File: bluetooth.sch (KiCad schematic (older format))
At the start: 4 parts

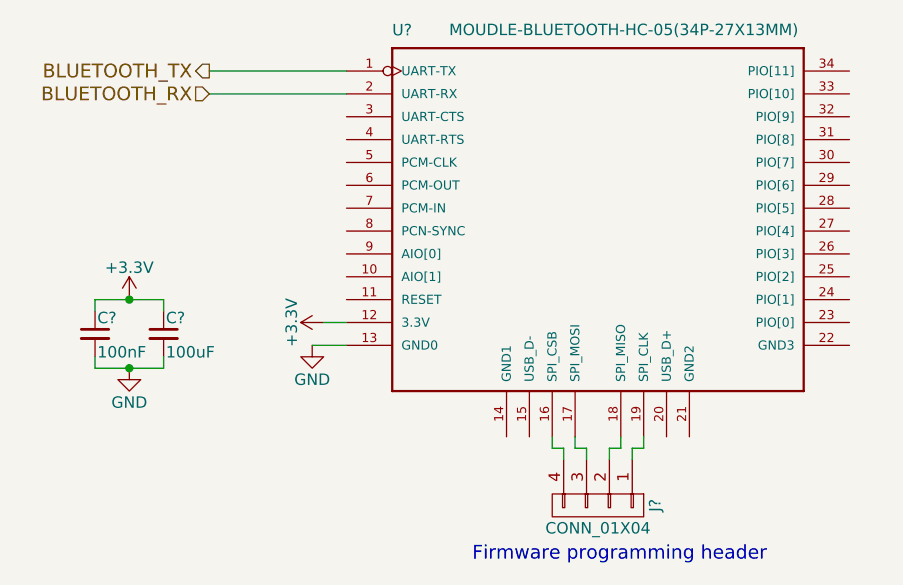
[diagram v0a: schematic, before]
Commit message: Make top-level connections between microcontroller and everything else
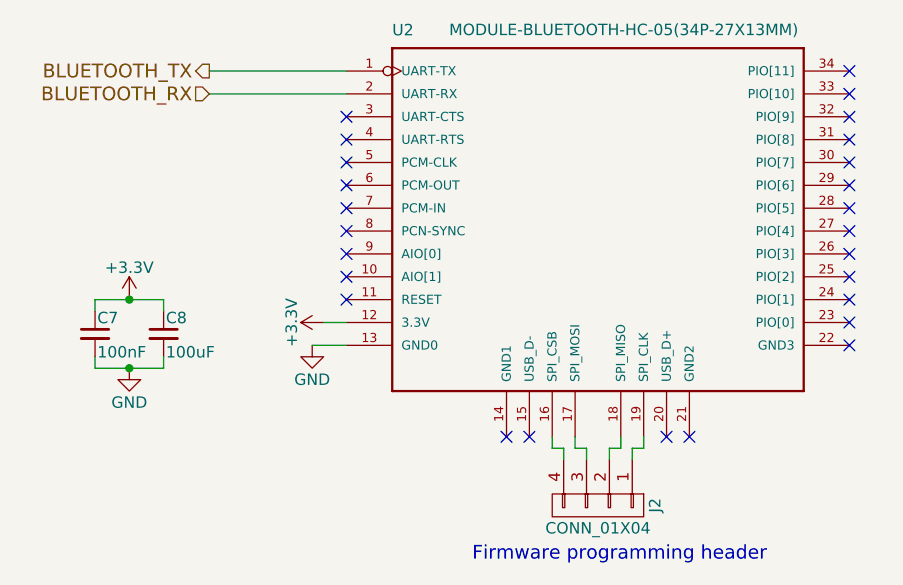
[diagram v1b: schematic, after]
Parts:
- U2: renamed from U?; value MOUDLE-BLUETOOTH-HC-05(34P-27X13MM) -> MODULE-BLUETOOTH-HC-05(34P-27X13MM); footprint BT34P-SMD-1.5-26.9X13.0X2.2MM -> (none)
- gave numbers to parts that had none: 3
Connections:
- no-connect marks 0 -> 26
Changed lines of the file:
@@
 $EndDescr
 $Comp
-L +3.3V #PWR?
+L +3.3V #PWR010
 U 1 1 599FF956
 P 4750 3550
-F 0 "#PWR?" H 4750 3400 50  0001 C CNN
+F 0 "#PWR010" H 4750 3400 50  0001 C CNN
 F 1 "+3.3V" H 4750 3690 50  0000 C CNN
 F 2 "" H 4750 3550 50  0001 C CNN
@@
 $EndComp
 $Comp
-L CONN_01X04 J?
+L CONN_01X04 J2
 U 1 1 599FF9B5
 P 5950 4350
-F 0 "J?" H 5950 4600 50  0000 C CNN
+F 0 "J2" H 5950 4600 50  0000 C CNN
 F 1 "CONN_01X04" V 6050 4350 50  0000 C CNN
 F 2 "" H 5950 4350 50  0001 C CNN
@@
 	4850 3550 4750 3550
 $Comp
-L GND #PWR?
+L GND #PWR011
 U 1 1 599FFB01
 P 4700 3650
-F 0 "#PWR?" H 4700 3400 50  0001 C CNN
+F 0 "#PWR011" H 4700 3400 50  0001 C CNN
 F 1 "GND" H 4700 3500 50  0000 C CNN
 F 2 "" H 4700 3650 50  0001 C CNN
@@
 BLUETOOTH_RX
 $Comp
-L C_Small C?
+L C_Small C8
 U 1 1 599FFDBC
 P 4050 3600
-F 0 "C?" H 4060 3670 50  0000 L CNN
+F 0 "C8" H 4060 3670 50  0000 L CNN
 F 1 "100uF" H 4060 3520 50  0000 L CNN
 F 2 "" H 4050 3600 50  0001 C CNN
@@
 $EndComp
 $Comp
-L C_Small C?
+L C_Small C7
 U 1 1 599FFE10
 P 3750 3600
-F 0 "C?" H 3760 3670 50  0000 L CNN
+F 0 "C7" H 3760 3670 50  0000 L CNN
 F 1 "100nF" H 3760 3520 50  0000 L CNN
 F 2 "" H 3750 3600 50  0001 C CNN
@@
 $EndComp
 $Comp
-L GND #PWR?
+L GND #PWR012
 U 1 1 599FFE4C
 P 3900 3750
-F 0 "#PWR?" H 3900 3500 50  0001 C CNN
+F 0 "#PWR012" H 3900 3500 50  0001 C CNN
 F 1 "GND" H 3900 3600 50  0000 C CNN
 F 2 "" H 3900 3750 50  0001 C CNN
@@
 $EndComp
 $Comp
-L +3.3V #PWR?
+L +3.3V #PWR013
 U 1 1 599FFE63
 P 3900 3450
-F 0 "#PWR?" H 3900 3300 50  0001 C CNN
+F 0 "#PWR013" H 3900 3300 50  0001 C CNN
 F 1 "+3.3V" H 3900 3590 50  0000 C CNN
 F 2 "" H 3900 3450 50  0001 C CNN
@@
 Connection ~ 3900 3450
 $Comp
-L MOUDLE-BLUETOOTH-HC-05(34P-27X13MM) U?
+L MOUDLE-BLUETOOTH-HC-05(34P-27X13MM) U2
 U 1 1 59A0DEC9
 P 5950 3100
-F 0 "U?" H 5050 3900 50  0000 L BNN
-F 1 "MOUDLE-BLUETOOTH-HC-05(34P-27X13MM)" H 5299 3901 50  0000 L BNN
-F 2 "BT34P-SMD-1.5-26.9X13.0X2.2MM" H 5950 3100 50  0001 L BNN
+F 0 "U2" H 5050 3900 50  0000 L BNN
+F 1 "MODULE-BLUETOOTH-HC-05(34P-27X13MM)" H 5299 3901 50  0000 L BNN
+F 2 "" H 5950 3100 50  0001 L BNN
 F 3 "None" H 5950 3100 50  0001 L BNN
 F 4 "HC-05" H 5950 3100 50  0001 L BNN "MP"
@@
 Text Notes 5400 4600 0    60   ~ 0
 Firmware programming header
+NoConn ~ 6350 4050
+NoConn ~ 6250 4050
+NoConn ~ 5650 4050
+NoConn ~ 5550 4050
+NoConn ~ 4850 3450
+NoConn ~ 4850 3350
+NoConn ~ 4850 3250
+NoConn ~ 4850 3150
+NoConn ~ 4850 3050
+NoConn ~ 4850 2950
+NoConn ~ 4850 2850
+NoConn ~ 4850 2750
+NoConn ~ 4850 2650
+NoConn ~ 7050 2450
+NoConn ~ 7050 2550
+NoConn ~ 7050 2650
+NoConn ~ 7050 2750
+NoConn ~ 7050 2850
+NoConn ~ 7050 2950
+NoConn ~ 7050 3050
+NoConn ~ 7050 3150
+NoConn ~ 7050 3250
+NoConn ~ 7050 3350
+NoConn ~ 7050 3450
+NoConn ~ 7050 3550
+NoConn ~ 7050 3650
 $EndSCHEMATC

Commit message: Assigned some footprints and added CR1225 holder footprint
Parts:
- C7: footprint (none) -> Capacitors_SMD:C_0603
- C8: footprint (none) -> Capacitors_Tantalum_SMD:CP_Tantalum_Case-B_EIA-3528-21_Reflow
- J2: footprint (none) -> Pin_Headers:Pin_Header_Straight_1x04_Pitch2.54mm
- U2: footprint (none) -> bluetooth_hc-05:BT34P-SMD-1.5-26.9X13.0X2.2MM
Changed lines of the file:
@@
 F 0 "J2" H 5950 4600 50  0000 C CNN
 F 1 "CONN_01X04" V 6050 4350 50  0000 C CNN
-F 2 "" H 5950 4350 50  0001 C CNN
+F 2 "Pin_Headers:Pin_Header_Straight_1x04_Pitch2.54mm" H 5950 4350 50  0001 C CNN
 F 3 "" H 5950 4350 50  0001 C CNN
 	1    5950 4350
@@
 F 0 "C8" H 4060 3670 50  0000 L CNN
 F 1 "100uF" H 4060 3520 50  0000 L CNN
-F 2 "" H 4050 3600 50  0001 C CNN
+F 2 "Capacitors_Tantalum_SMD:CP_Tantalum_Case-B_EIA-3528-21_Reflow" H 4050 3600 50  0001 C CNN
 F 3 "" H 4050 3600 50  0001 C CNN
 	1    4050 3600
@@
 F 0 "C7" H 3760 3670 50  0000 L CNN
 F 1 "100nF" H 3760 3520 50  0000 L CNN
-F 2 "" H 3750 3600 50  0001 C CNN
+F 2 "Capacitors_SMD:C_0603" H 3750 3600 50  0001 C CNN
 F 3 "" H 3750 3600 50  0001 C CNN
 	1    3750 3600
@@
 F 0 "U2" H 5050 3900 50  0000 L BNN
 F 1 "MODULE-BLUETOOTH-HC-05(34P-27X13MM)" H 5299 3901 50  0000 L BNN
-F 2 "" H 5950 3100 50  0001 L BNN
+F 2 "bluetooth_hc-05:BT34P-SMD-1.5-26.9X13.0X2.2MM" H 5950 3100 50  0001 L BNN
 F 3 "None" H 5950 3100 50  0001 L BNN
 F 4 "HC-05" H 5950 3100 50  0001 L BNN "MP"

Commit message: Create relevant BOM links, export digikey BOM
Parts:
- C8: MFR (none) -> AVX; MPN (none) -> F930J107MBA; SPN (none) -> 478-8156-1-ND; SPR (none) -> https://www.digikey.com.au/
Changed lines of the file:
@@
 U 1 1 599FF956
 P 4750 3550
-F 0 "#PWR010" H 4750 3400 50  0001 C CNN
-F 1 "+3.3V" H 4750 3690 50  0000 C CNN
-F 2 "" H 4750 3550 50  0001 C CNN
-F 3 "" H 4750 3550 50  0001 C CNN
+F 0 "#PWR010" H 4750 3400 50 0001 C CNN
+F 1 "+3.3V" H 4750 3690 50 0000 C CNN
+F 2 "" H 4750 3550 50 0001 C CNN
+F 3 "" H 4750 3550 50 0001 C CNN
 	1    4750 3550
 	0    -1   -1   0
@@
 U 1 1 599FF9B5
 P 5950 4350
-F 0 "J2" H 5950 4600 50  0000 C CNN
-F 1 "CONN_01X04" V 6050 4350 50  0000 C CNN
-F 2 "Pin_Headers:Pin_Header_Straight_1x04_Pitch2.54mm" H 5950 4350 50  0001 C CNN
-F 3 "" H 5950 4350 50  0001 C CNN
+F 0 "J2" H 5950 4600 50 0000 C CNN
+F 1 "CONN_01X04" V 6050 4350 50 0000 C CNN
+F 2 "Pin_Headers:Pin_Header_Straight_1x04_Pitch2.54mm" H 5950 4350 50 0001 C CNN
+F 3 "" H 5950 4350 50 0001 C CNN
+F 4 "" H 0 0 50 0001 C CNN "MFR"
+F 5 "" H 0 0 50 0001 C CNN "MPN"
+F 6 "" H 0 0 50 0001 C CNN "SPR"
+F 7 "" H 0 0 50 0001 C CNN "SPN"
+F 8 "" H 0 0 50 0001 C CNN "SPURL"
 	1    5950 4350
 	0    1    1    0
 $EndComp
+$Comp
+L GND #PWR011
+U 1 1 599FFB01
+P 4700 3650
+F 0 "#PWR011" H 4700 3400 50 0001 C CNN
+F 1 "GND" H 4700 3500 50 0000 C CNN
+F 2 "" H 4700 3650 50 0001 C CNN
+F 3 "" H 4700 3650 50 0001 C CNN
+	1    4700 3650
+	1    0    0    -1
+$EndComp
+$Comp
+L C_Small C8
+U 1 1 599FFDBC
+P 4050 3600
+F 0 "C8" H 4060 3670 50 0000 L CNN
+F 1 "100uF" H 4060 3520 50 0000 L CNN
+F 2 "Capacitors_Tantalum_SMD:CP_Tantalum_Case-B_EIA-3528-21_Reflow" H 4050 3600 50 0001 C CNN
+F 3 "http://datasheets.avx.com/F93.pdf" H 4050 3600 50 0001 C CNN
+F 4 "AVX" H 0 0 50 0001 C CNN "MFR"
+F 5 "F930J107MBA" H 0 0 50 0001 C CNN "MPN"
+F 6 "https://www.digikey.com.au/" H 0 0 50 0001 C CNN "SPR"
+F 7 "478-8156-1-ND" H 0 0 50 0001 C CNN "SPN"
+F 8 "" H 0 0 50 0001 C CNN "SPURL"
+	1    4050 3600
+	1    0    0    -1
+$EndComp
+$Comp
+L C_Small C7
+U 1 1 599FFE10
+P 3750 3600
+F 0 "C7" H 3760 3670 50 0000 L CNN
+F 1 "100nF" H 3760 3520 50 0000 L CNN
+F 2 "Capacitors_SMD:C_0603" H 3750 3600 50 0001 C CNN
+F 3 "" H 3750 3600 50 0001 C CNN
+F 4 "" H 0 0 50 0001 C CNN "MFR"
+F 5 "" H 0 0 50 0001 C CNN "MPN"
+F 6 "" H 0 0 50 0001 C CNN "SPR"
+F 7 "" H 0 0 50 0001 C CNN "SPN"
+F 8 "" H 0 0 50 0001 C CNN "SPURL"
+	1    3750 3600
+	1    0    0    -1
+$EndComp
+$Comp
+L GND #PWR012
+U 1 1 599FFE4C
+P 3900 3750
+F 0 "#PWR012" H 3900 3500 50 0001 C CNN
+F 1 "GND" H 3900 3600 50 0000 C CNN
+F 2 "" H 3900 3750 50 0001 C CNN
+F 3 "" H 3900 3750 50 0001 C CNN
+	1    3900 3750
+	1    0    0    -1
+$EndComp
+$Comp
+L +3.3V #PWR013
+U 1 1 599FFE63
+P 3900 3450
+F 0 "#PWR013" H 3900 3300 50 0001 C CNN
+F 1 "+3.3V" H 3900 3590 50 0000 C CNN
+F 2 "" H 3900 3450 50 0001 C CNN
+F 3 "" H 3900 3450 50 0001 C CNN
+	1    3900 3450
+	1    0    0    -1
+$EndComp
+$Comp
+L MOUDLE-BLUETOOTH-HC-05(34P-27X13MM) U2
+U 1 1 59A0DEC9
+P 5950 3100
+F 0 "U2" H 5050 3900 50 0000 L BNN
+F 1 "MODULE-BLUETOOTH-HC-05(34P-27X13MM)" H 5299 3901 50 0000 L BNN
+F 2 "bluetooth_hc-05:BT34P-SMD-1.5-26.9X13.0X2.2MM" H 5950 3100 50 0001 L BNN
+F 3 "None" H 5950 3100 50 0001 L BNN
+F 4 "HC-05" H 5950 3100 50 0001 L BNN "MP"
+F 5 "SOIC-14 " H 5950 3100 50 0001 L BNN "Package"
+F 6 "Unavailable" H 5950 3100 50 0001 L BNN "Availability"
+F 7 "None" H 5950 3100 50 0001 L BNN "Description"
+F 8 "" H 5950 3100 50 0001 L BNN "MF"
+F 9 "" H 0 0 50 0001 C CNN "MFR"
+F 10 "" H 0 0 50 0001 C CNN "MPN"
+F 11 "" H 0 0 50 0001 C CNN "SPR"
+F 12 "" H 0 0 50 0001 C CNN "SPN"
+F 13 "" H 0 0 50 0001 C CNN "SPURL"
+	1    5950 3100
+	1    0    0    -1
+$EndComp
+Text HLabel 4250 2450 0    60   Output ~ 0
+BLUETOOTH_TX
+Text HLabel 4250 2550 0    60   Input ~ 0
+BLUETOOTH_RX
+Text Notes 5400 4600 0    60   ~ 0
+Firmware programming header
 Wire Wire Line
 	6150 4050 6150 4100
@@
 Wire Wire Line
 	4850 3550 4750 3550
-$Comp
-L GND #PWR011
-U 1 1 599FFB01
-P 4700 3650
-F 0 "#PWR011" H 4700 3400 50  0001 C CNN
-F 1 "GND" H 4700 3500 50  0000 C CNN
-F 2 "" H 4700 3650 50  0001 C CNN
-F 3 "" H 4700 3650 50  0001 C CNN
-	1    4700 3650
-	1    0    0    -1
-$EndComp
 Wire Wire Line
 	4850 3650 4700 3650
@@
 Wire Wire Line
 	4850 2550 4250 2550
-Text HLabel 4250 2450 0    60   Output ~ 0
-BLUETOOTH_TX
-Text HLabel 4250 2550 0    60   Input ~ 0
-BLUETOOTH_RX
-$Comp
-L C_Small C8
-U 1 1 599FFDBC
-P 4050 3600
-F 0 "C8" H 4060 3670 50  0000 L CNN
-F 1 "100uF" H 4060 3520 50  0000 L CNN
-F 2 "Capacitors_Tantalum_SMD:CP_Tantalum_Case-B_EIA-3528-21_Reflow" H 4050 3600 50  0001 C CNN
-F 3 "" H 4050 3600 50  0001 C CNN
-	1    4050 3600
-	1    0    0    -1
-$EndComp
-$Comp
-L C_Small C7
-U 1 1 599FFE10
-P 3750 3600
-F 0 "C7" H 3760 3670 50  0000 L CNN
-F 1 "100nF" H 3760 3520 50  0000 L CNN
-F 2 "Capacitors_SMD:C_0603" H 3750 3600 50  0001 C CNN
-F 3 "" H 3750 3600 50  0001 C CNN
-	1    3750 3600
-	1    0    0    -1
-$EndComp
-$Comp
-L GND #PWR012
-U 1 1 599FFE4C
-P 3900 3750
-F 0 "#PWR012" H 3900 3500 50  0001 C CNN
-F 1 "GND" H 3900 3600 50  0000 C CNN
-F 2 "" H 3900 3750 50  0001 C CNN
-F 3 "" H 3900 3750 50  0001 C CNN
-	1    3900 3750
-	1    0    0    -1
-$EndComp
-$Comp
-L +3.3V #PWR013
-U 1 1 599FFE63
-P 3900 3450
-F 0 "#PWR013" H 3900 3300 50  0001 C CNN
-F 1 "+3.3V" H 3900 3590 50  0000 C CNN
-F 2 "" H 3900 3450 50  0001 C CNN
-F 3 "" H 3900 3450 50  0001 C CNN
-	1    3900 3450
-	1    0    0    -1
-$EndComp
 Wire Wire Line
 	3750 3700 3750 3750
 Wire Wire Line
 	3750 3750 4050 3750
-Connection ~ 3900 3750
 Wire Wire Line
 	4050 3750 4050 3700
@@
 Wire Wire Line
 	3750 3450 3750 3500
+Connection ~ 3900 3750
 Connection ~ 3900 3450
-$Comp
-L MOUDLE-BLUETOOTH-HC-05(34P-27X13MM) U2
-U 1 1 59A0DEC9
-P 5950 3100
-F 0 "U2" H 5050 3900 50  0000 L BNN
-F 1 "MODULE-BLUETOOTH-HC-05(34P-27X13MM)" H 5299 3901 50  0000 L BNN
-F 2 "bluetooth_hc-05:BT34P-SMD-1.5-26.9X13.0X2.2MM" H 5950 3100 50  0001 L BNN
-F 3 "None" H 5950 3100 50  0001 L BNN
-F 4 "HC-05" H 5950 3100 50  0001 L BNN "MP"
-F 5 "SOIC-14 " H 5950 3100 50  0001 L BNN "Package"
-F 6 "Unavailable" H 5950 3100 50  0001 L BNN "Availability"
-F 7 "None" H 5950 3100 50  0001 L BNN "Description"
-F 8 "" H 5950 3100 50  0001 L BNN "MF"
-	1    5950 3100
-	1    0    0    -1
-$EndComp
-Text Notes 5400 4600 0    60   ~ 0
-Firmware programming header
 NoConn ~ 6350 4050
 NoConn ~ 6250 4050
